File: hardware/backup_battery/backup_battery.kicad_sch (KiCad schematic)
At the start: 8 parts, among them U1 MCP1700x-330xxMB

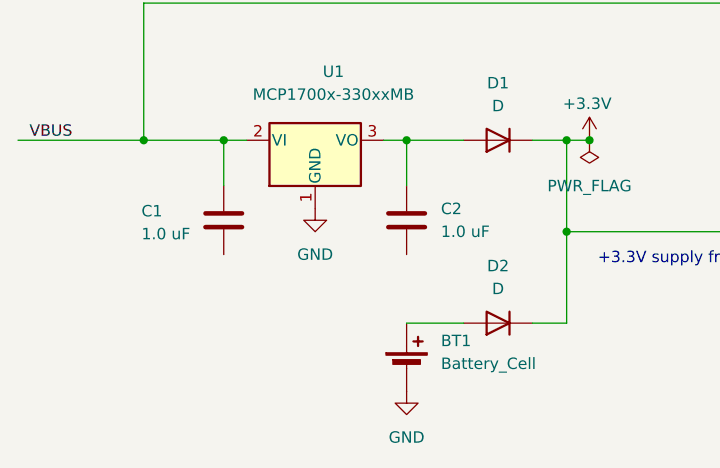
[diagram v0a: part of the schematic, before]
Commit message: Add missing ground connections in regulator circuit
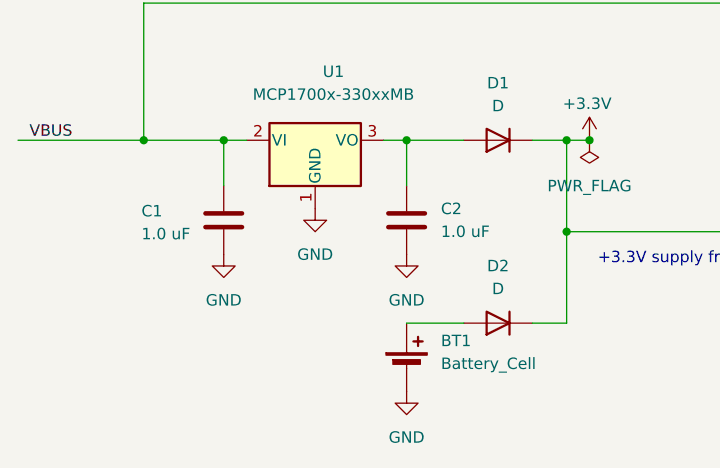
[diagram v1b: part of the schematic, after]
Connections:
- net GND: now also C1.2, C2.2
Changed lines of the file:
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@@
+	)
+	(symbol
+		(lib_id "power:GND")
+		(at 104.14 87.63 0)
+		(unit 1)
+		(exclude_from_sim no)
+		(in_bom yes)
+		(on_board yes)
+		(dnp no)
+		(fields_autoplaced yes)
+		(property "Reference" "#PWR06"
+			(at 104.14 93.98 0)
+			(effects
+				(font
+					(size 1.27 1.27)
+				)
+				(hide yes)
+			)
+		)
+		(property "Value" "GND"
+			(at 104.14 92.71 0)
+			(effects
+				(font
+					(size 1.27 1.27)
+				)
+			)
+		)
+		(property "Footprint" ""
+			(at 104.14 87.63 0)
+			(effects
+				(font
+					(size 1.27 1.27)
+				)
+				(hide yes)
+			)
+		)
+		(property "Datasheet" ""
+			(at 104.14 87.63 0)
+			(effects
+				(font
+					(size 1.27 1.27)
+				)
+				(hide yes)
+			)
+		)
+		(property "Description" "Power symbol creates a global label with name \"GND\" , ground"
+			(at 104.14 87.63 0)
+			(effects
+				(font
+					(size 1.27 1.27)
+				)
+				(hide yes)
+			)
+		)
+		(pin "1"
+		)
+		(instances
+			(project "backup_battery"
+				(path "/4a8fbeeb-60dc-48a5-8d5a-b7508ae82810"
+					(reference "#PWR06")
+					(unit 1)
+				)
+			)
+		)
 	)
 	(symbol
@@
 					(unit 1)
 				)
+			)
+		)
+	)
+	(symbol
+		(lib_id "power:GND")
+		(at 83.82 87.63 0)
+		(unit 1)
+		(exclude_from_sim no)
+		(in_bom yes)
+		(on_board yes)
+		(dnp no)
+		(fields_autoplaced yes)
+		(property "Reference" "#PWR05"
+			(at 83.82 93.98 0)
+			(effects
+				(font
+					(size 1.27 1.27)
+				)
+				(hide yes)
+			)
+		)
+		(property "Value" "GND"
+			(at 83.82 92.71 0)
+			(effects
+				(font
+					(size 1.27 1.27)
+				)
+			)
+		)
+		(property "Footprint" ""
+			(at 83.82 87.63 0)
+			(effects
+				(font
+					(size 1.27 1.27)
+				)
+				(hide yes)
+			)
+		)
+		(property "Datasheet" ""
+			(at 83.82 87.63 0)
+			(effects
+				(font
+					(size 1.27 1.27)
+				)
+				(hide yes)
+			)
+		)
+		(property "Description" "Power symbol creates a global label with name \"GND\" , ground"
+			(at 83.82 87.63 0)
+			(effects
+				(font
+					(size 1.27 1.27)
+				)
+				(hide yes)
+			)
+		)
+		(pin "1"
+		)
+		(instances
+			(project "backup_battery"
+				(path "/4a8fbeeb-60dc-48a5-8d5a-b7508ae82810"
+					(reference "#PWR05")
+					(unit 1)
+				)

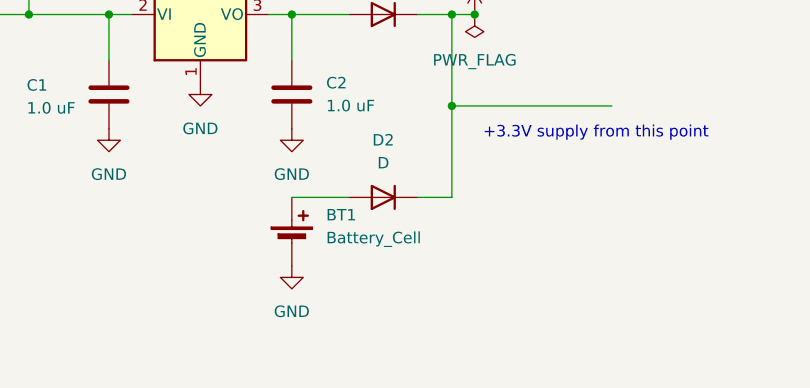
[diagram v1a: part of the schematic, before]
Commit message: Change battery holder, add footprint and symbol
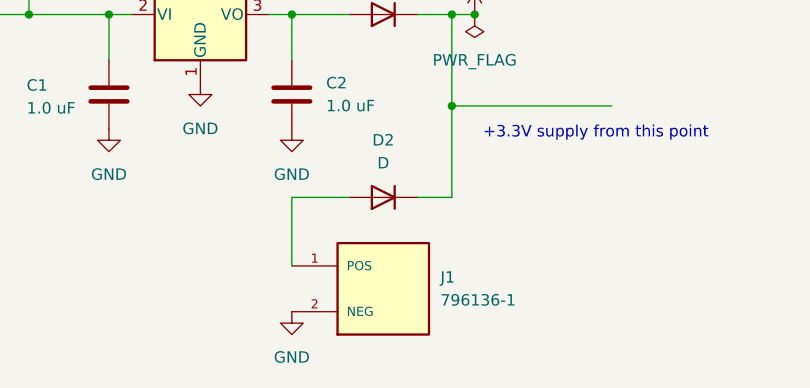
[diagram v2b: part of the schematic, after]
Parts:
- removed BT1: Battery_Cell, symbol Device:Battery_Cell
- added J1: 796136-1, 796136-1:TE_796136-1, symbol 796136-1:796136-1
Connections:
- net GND: now also J1.2 (NEG)
- net at D2.2 (A): now also J1.1 (POS)
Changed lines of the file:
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@@
+	(wire
+		(pts
+			(xy 104.14 95.25) (xy 104.14 102.87)
+		)
+		(stroke
+			(width 0)
+			(type default)
+		)
+	)
 	(wire
 		(pts
@@
 	)
 	(symbol
+		(lib_id "power:GND")
+		(at 104.14 107.95 0)
+		(unit 1)
+		(exclude_from_sim no)
+		(in_bom yes)
+		(on_board yes)
+		(dnp no)
+		(fields_autoplaced yes)
+		(property "Reference" "#PWR03"
+			(at 104.14 114.3 0)
+			(effects
+				(font
+					(size 1.27 1.27)
+				)
+				(hide yes)
+			)
+		)
+		(property "Value" "GND"
+			(at 104.14 113.03 0)
+			(effects
+				(font
+					(size 1.27 1.27)
+				)
+			)
+		)
+		(property "Footprint" ""
+			(at 104.14 107.95 0)
+			(effects
+				(font
+					(size 1.27 1.27)
+				)
+				(hide yes)
+			)
+		)
+		(property "Datasheet" ""
+			(at 104.14 107.95 0)
+			(effects
+				(font
+					(size 1.27 1.27)
+				)
+				(hide yes)
+			)
+		)
+		(property "Description" "Power symbol creates a global label with name \"GND\" , ground"
+			(at 104.14 107.95 0)
+			(effects
+				(font
+					(size 1.27 1.27)
+				)
+				(hide yes)
+			)
+		)
+		(pin "1"
+		)
+		(instances
+			(project "backup_battery"
+				(path "/4a8fbeeb-60dc-48a5-8d5a-b7508ae82810"
+					(reference "#PWR03")
+					(unit 1)
+				)
+			)
+		)
+	)
+	(symbol
 		(lib_id "power:PWR_FLAG")
 		(at 124.46 74.93 180)
@@
 	)
 	(symbol
-		(lib_id "Device:Battery_Cell")
-		(at 104.14 100.33 0)
+		(lib_id "796136-1:796136-1")
+		(at 114.3 105.41 0)
 		(unit 1)
 		(exclude_from_sim no)
@@
 		(dnp no)
 		(fields_autoplaced yes)
-		(property "Reference" "BT1"
-			(at 107.95 97.2184 0)
+		(property "Reference" "J1"
+			(at 120.65 104.1399 0)
 			(effects
 				(font
@@
 			)
 		)
-		(property "Value" "Battery_Cell"
-			(at 107.95 99.7584 0)
+		(property "Value" "796136-1"
+			(at 120.65 106.6799 0)
 			(effects
 				(font
@@
 			)
 		)
-		(property "Footprint" ""
-			(at 104.14 98.806 90)
-			(effects
-				(font
-					(size 1.27 1.27)
-				)
-				(hide yes)
-			)
-		)
-		(property "Datasheet" "~"
-			(at 104.14 98.806 90)
-			(effects
-				(font
-					(size 1.27 1.27)
-				)
-				(hide yes)
-			)
-		)
-		(property "Description" "Single-cell battery"
-			(at 104.14 100.33 0)
-			(effects
-				(font
-					(size 1.27 1.27)
-				)
+		(property "Footprint" "796136-1:TE_796136-1"
+			(at 114.3 105.41 0)
+			(effects
+				(font
+					(size 1.27 1.27)
+				)
+				(justify bottom)
+				(hide yes)
+			)
+		)
+		(property "Datasheet" ""
+			(at 114.3 105.41 0)
+			(effects
+				(font
+					(size 1.27 1.27)
+				)
+				(hide yes)
+			)
+		)
+		(property "Description" ""
+			(at 114.3 105.41 0)
+			(effects
+				(font
+					(size 1.27 1.27)
+				)
+				(hide yes)
+			)
+		)
+		(property "Comment" "796136-1"
+			(at 114.3 105.41 0)
+			(effects
+				(font
+					(size 1.27 1.27)
+				)
+				(justify bottom)
+				(hide yes)
+			)
+		)
+		(property "MF" "TE Connectivity"
+			(at 114.3 105.41 0)
+			(effects
+				(font
+					(size 1.27 1.27)
+				)
+				(justify bottom)
+				(hide yes)
+			)
+		)
+		(property "Description_1" "\n                        \n                            Surface Mount Battery Holder For 1, Leaf Spring Contact | TE Connectivity 796136-1\n                        \n"
+			(at 114.3 105.41 0)
+			(effects
+				(font
+					(size 1.27 1.27)
+				)
+				(justify bottom)
+				(hide yes)
+			)
+		)
+		(property "Package" "CR 2032 Battery Holder TE Connectivity"
+			(at 114.3 105.41 0)
+			(effects
+				(font
+					(size 1.27 1.27)
+				)
+				(justify bottom)
+				(hide yes)
+			)
+		)
+		(property "Price" "None"
+			(at 114.3 105.41 0)
+			(effects
+				(font
+					(size 1.27 1.27)
+				)
+				(justify bottom)
+				(hide yes)
+			)
+		)
+		(property "Check_prices" "https://www.snapeda.com/parts/796136-1/TE+Connectivity+AMP+Connectors/view-part/?ref=eda"
+			(at 114.3 105.41 0)
+			(effects
+				(font
+					(size 1.27 1.27)
+				)
+				(justify bottom)
+				(hide yes)
+			)
+		)
+		(property "STANDARD" "Manufacturer Recommendations"
+			(at 114.3 105.41 0)
+			(effects
+				(font
+					(size 1.27 1.27)
+				)
+				(justify bottom)
+				(hide yes)
+			)
+		)
+		(property "PARTREV" "G2"
+			(at 114.3 105.41 0)
+			(effects
+				(font
+					(size 1.27 1.27)
+				)
+				(justify bottom)
+				(hide yes)
+			)
+		)
+		(property "SnapEDA_Link" "https://www.snapeda.com/parts/796136-1/TE+Connectivity+AMP+Connectors/view-part/?ref=snap"
+			(at 114.3 105.41 0)
+			(effects
+				(font
+					(size 1.27 1.27)
+				)
+				(justify bottom)
+				(hide yes)
+			)
+		)
+		(property "MP" "796136-1"
+			(at 114.3 105.41 0)
+			(effects
+				(font
+					(size 1.27 1.27)
+				)
+				(justify bottom)
+				(hide yes)
+			)
+		)
+		(property "Availability" "In Stock"
+			(at 114.3 105.41 0)
+			(effects
+				(font
+					(size 1.27 1.27)
+				)
+				(justify bottom)
+				(hide yes)
+			)
+		)
+		(property "MANUFACTURER" "TE CONNECTIVITY"
+			(at 114.3 105.41 0)
+			(effects
+				(font
+					(size 1.27 1.27)
+				)
+				(justify bottom)
 				(hide yes)
 			)
@@
 			(project ""
 				(path "/4a8fbeeb-60dc-48a5-8d5a-b7508ae82810"
-					(reference "BT1")
+					(reference "J1")
 					(unit 1)
 				)
@@
 					(unit 1)
 				)
-			)
-		)
-	)
-	(symbol
-		(lib_id "power:GND")
-		(at 104.14 102.87 0)
-		(unit 1)
-		(exclude_from_sim no)
-		(in_bom yes)
-		(on_board yes)
-		(dnp no)
-		(fields_autoplaced yes)
-		(property "Reference" "#PWR03"
-			(at 104.14 109.22 0)
-			(effects
-				(font
-					(size 1.27 1.27)
-				)
-				(hide yes)
-			)
-		)
-		(property "Value" "GND"
-			(at 104.14 107.95 0)
-			(effects
-				(font
-					(size 1.27 1.27)
-				)
-			)
-		)
-		(property "Footprint" ""
-			(at 104.14 102.87 0)
-			(effects
-				(font
-					(size 1.27 1.27)
-				)
-				(hide yes)
-			)
-		)
-		(property "Datasheet" ""
-			(at 104.14 102.87 0)
-			(effects
-				(font
-					(size 1.27 1.27)
-				)
-				(hide yes)
-			)
-		)
-		(property "Description" "Power symbol creates a global label with name \"GND\" , ground"
-			(at 104.14 102.87 0)
-			(effects
-				(font
-					(size 1.27 1.27)
-				)
-				(hide yes)
-			)
-		)
-		(pin "1"
-		)
-		(instances
-			(project "backup_battery_hw"
-				(path "/4a8fbeeb-60dc-48a5-8d5a-b7508ae82810"
-					(reference "#PWR03")
-					(unit 1)
-				)
